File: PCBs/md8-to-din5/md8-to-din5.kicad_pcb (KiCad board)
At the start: 2 copper layers, 32.6 x 28.8 mm, 6 parts, among them J1 DIN-5_180degree_female, J2 Mini-DIN-8_male, J3 RX/TX straight/null, J4 DTR/DSR straight/null

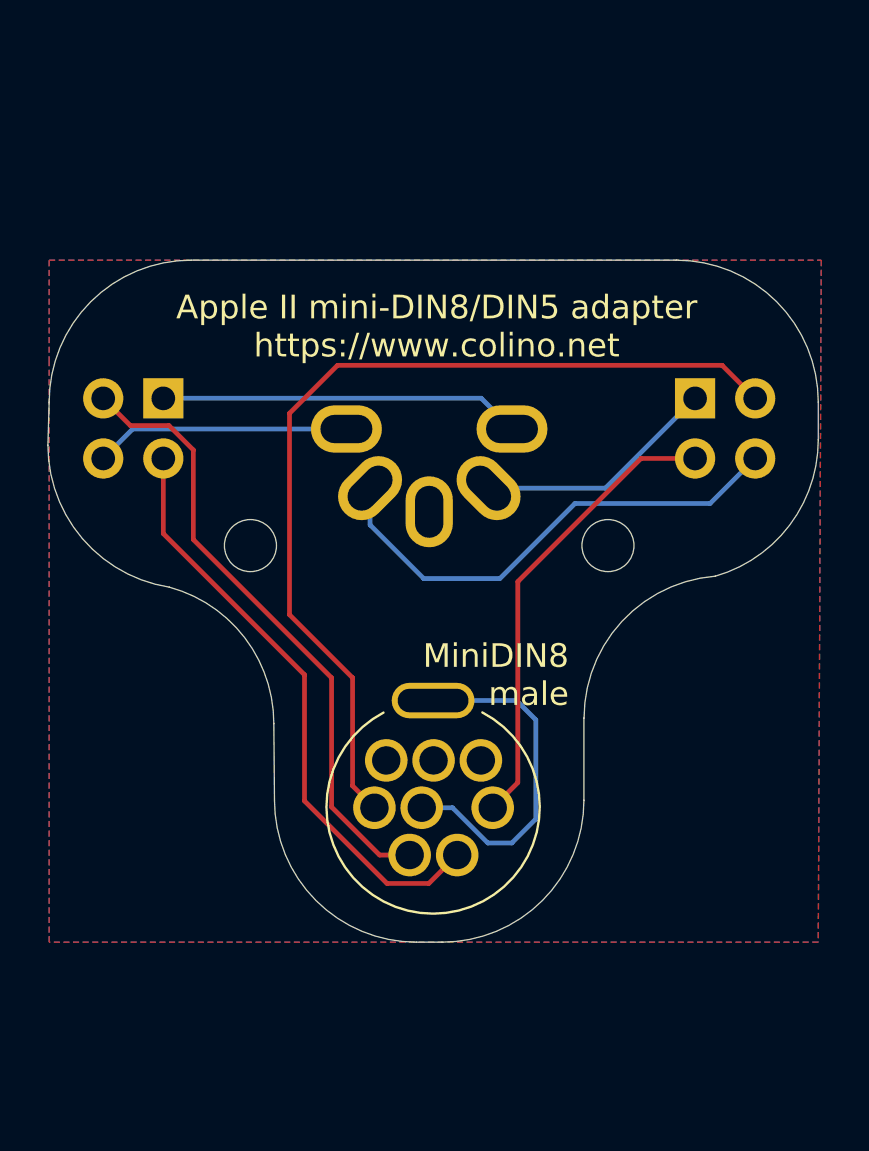
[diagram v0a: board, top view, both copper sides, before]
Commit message: Put traces on the other side of components
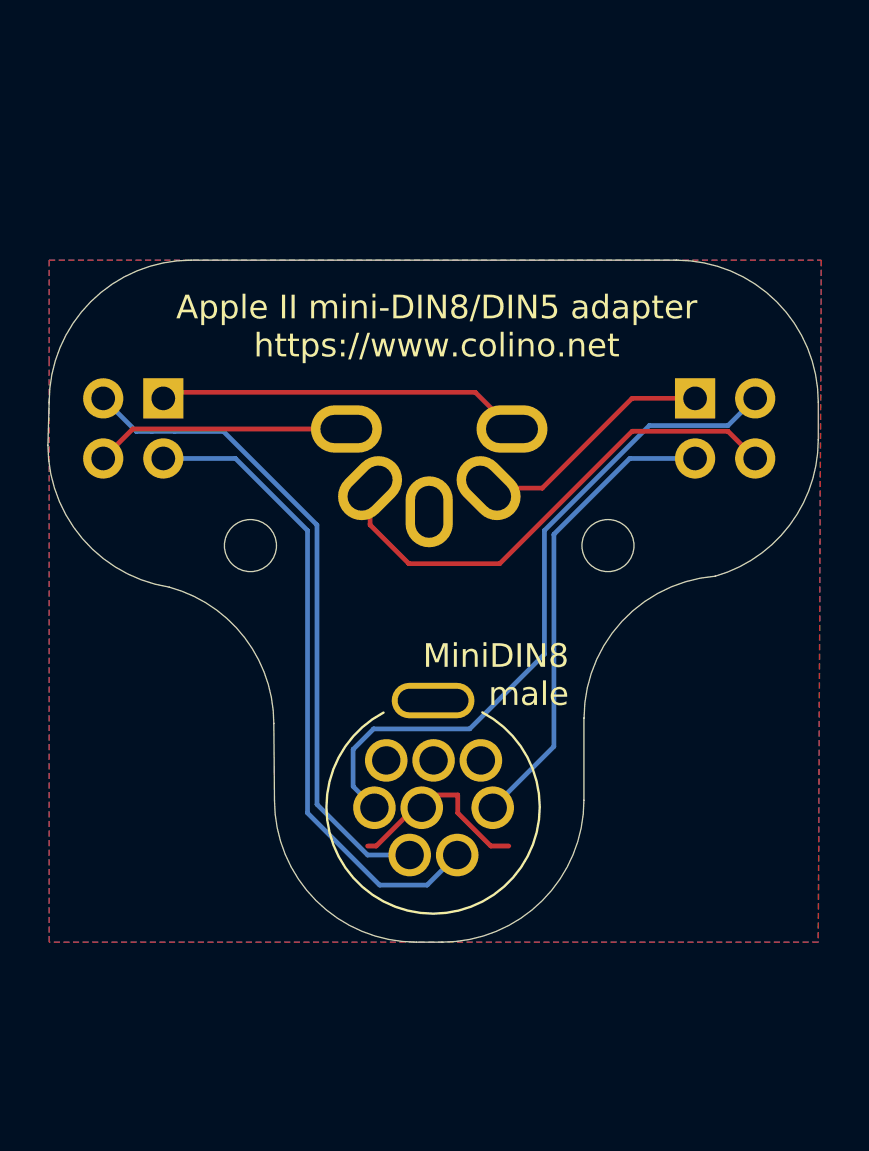
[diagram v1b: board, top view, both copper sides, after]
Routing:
- net Net-(J3-Pin_3): track 39.3 -> 29.0 mm
- net GND: track 14.7 -> 8.20 mm
- net Net-(J4-Pin_3): track 25.3 -> 27.4 mm
- net Net-(J4-Pin_2): track 26.4 -> 27.9 mm

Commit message: Fix silkscreen
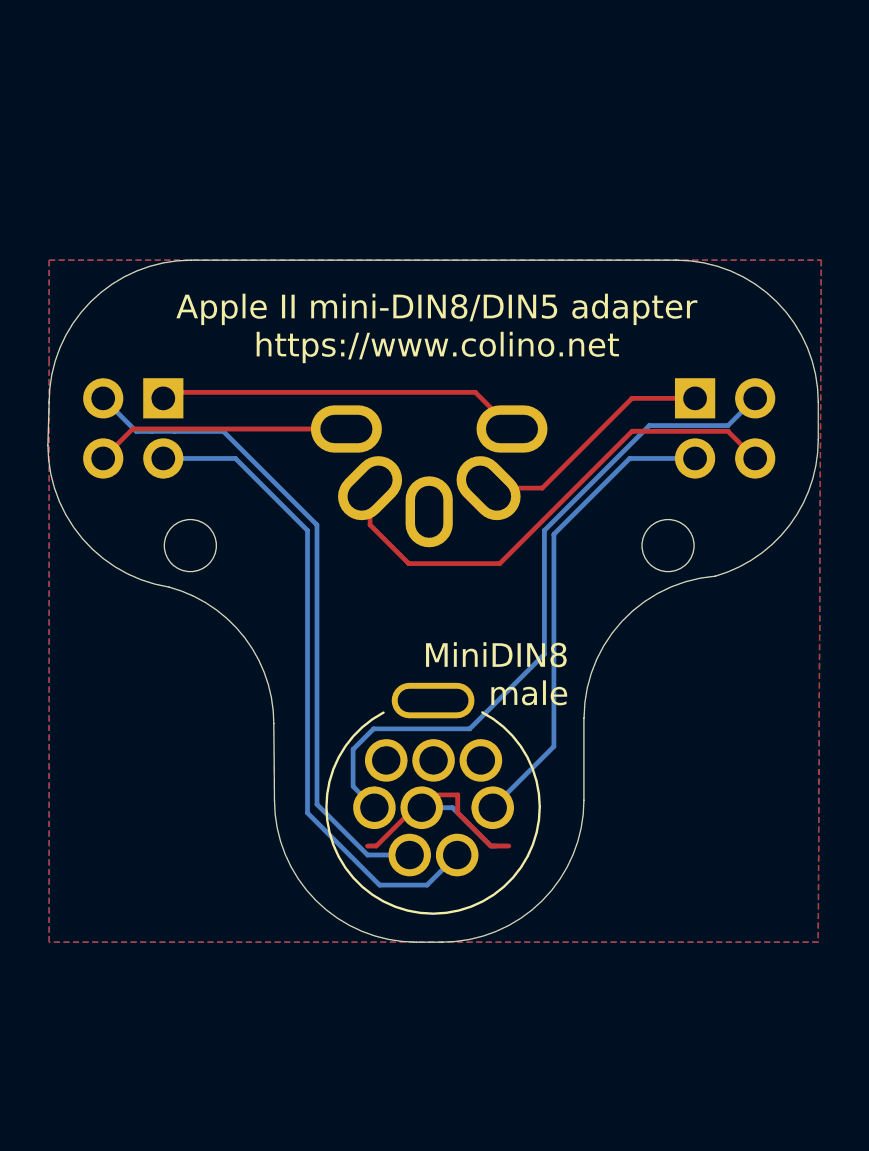
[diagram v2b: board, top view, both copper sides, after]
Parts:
- moved REF** 2.54 mm to (173.7, 97.7)
- moved REF** 2.54 mm to (193.9, 97.7)
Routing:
- net GND: track 8.20 -> 12.0 mm
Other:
- board text added: "↕ straight ↔ cross"
- board text removed: "↔ straight ↕ cross"
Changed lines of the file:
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@@
 	(footprint "MountingHole:MountingHole_2.2mm_M2_ISO7380"
 		(layer "F.Cu")
-		(at 191.389 97.663)
+		(at 193.929 97.663)
 		(descr "Mounting Hole 2.2mm, no annular, M2, ISO7380")
 		(tags "mounting hole 2.2mm no annular m2 iso7380")
@@
 	(footprint "MountingHole:MountingHole_2.2mm_M2_ISO7380"
 		(layer "F.Cu")
-		(at 176.276 97.663)
+		(at 173.736 97.663)
 		(descr "Mounting Hole 2.2mm, no annular, M2, ISO7380")
 		(tags "mounting hole 2.2mm no annular m2 iso7380")
@@
 		)
 	)
-	(gr_text "↔ straight\n↕ cross"
+	(gr_text "↕ straight\n↔ cross"
 		(at 196.342 89.408 0)
 		(layer "B.SilkS")
@@
 		(net 12)
 	)
+	(segment
+		(start 186.438943 110.363)
+		(end 186.69 110.363)
+		(width 0.2)
+		(layer "B.Cu")
+		(net 12)
+	)
+	(segment
+		(start 184.819943 108.744)
+		(end 186.438943 110.363)
+		(width 0.2)
+		(layer "B.Cu")
+		(net 12)
+	)
+	(segment
+		(start 183.517 108.744)
+		(end 184.819943 108.744)
+		(width 0.2)
+		(layer "B.Cu")
+		(net 12)
+	)

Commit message: Rework form factor for IIgs compatibility
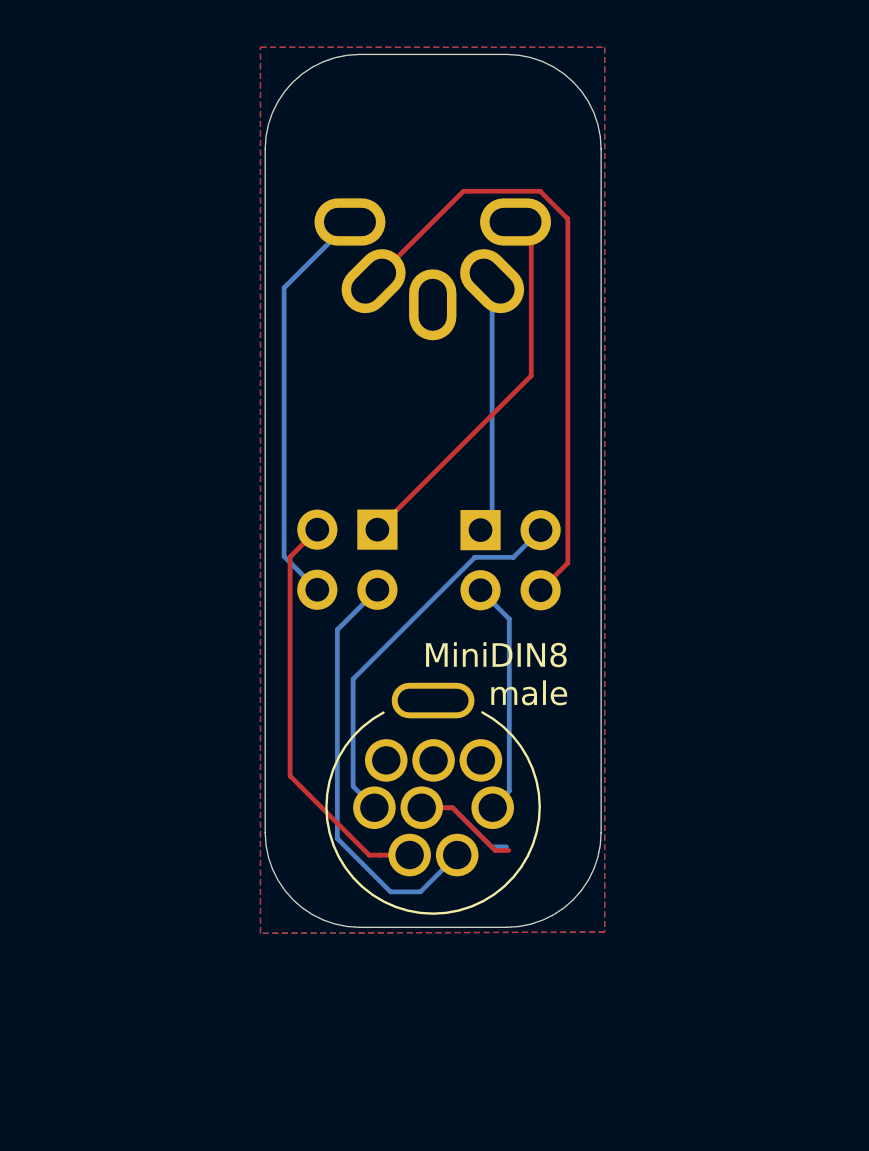
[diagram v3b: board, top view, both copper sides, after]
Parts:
- removed REF** (x2): MountingHole_2.2mm_M2_ISO7380, MountingHole:MountingHole_2.2mm_M2_ISO7380
- moved J3 10.6 mm to (186.0, 97.0)
- moved J4 10.6 mm to (181.6, 97.0)
- moved J1 8.75 mm to (184.0, 87.5)
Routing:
- net Net-(J3-Pin_3): track 29.0 -> 16.3 mm
- net Net-(J4-Pin_2): track 27.9 -> 17.3 mm
- net Net-(J3-Pin_2): track 19.9 -> 9.99 mm
- net Net-(J4-Pin_3): track 27.4 -> 17.9 mm
- net Net-(J4-Pin_4): track 10.8 -> 17.3 mm
- net Net-(J3-Pin_4): track 21.3 -> 26.4 mm
- net GND: track 12.0 -> 8.70 mm
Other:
- board size 32.6 x 28.8 mm -> 14.2 x 36.9 mm
- board text removed: "Apple II mini-DIN8/DIN5 adapter https://www.colino.net"

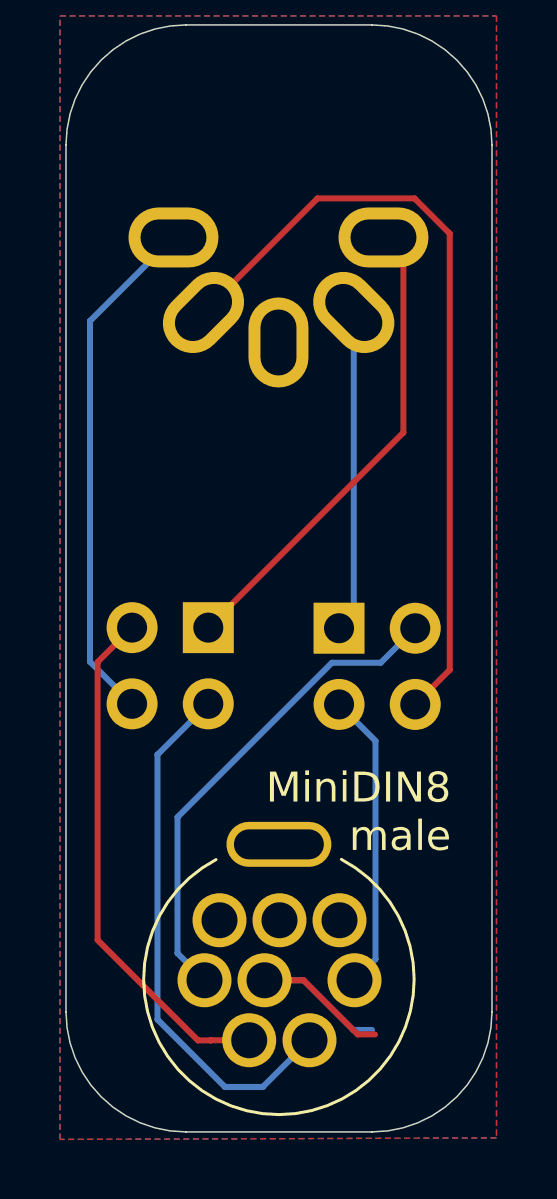
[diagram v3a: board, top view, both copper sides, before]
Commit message: Add switch to CISD
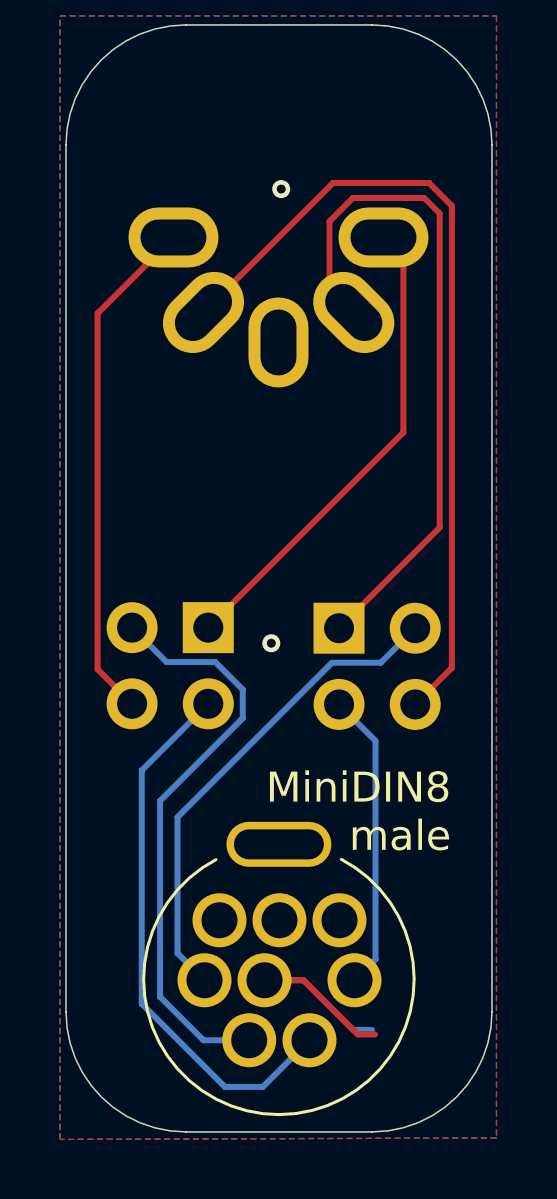
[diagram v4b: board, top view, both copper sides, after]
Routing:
- net Net-(J3-Pin_1): track 10.7 -> 22.8 mm
- net Net-(J4-Pin_2): track 17.3 -> 19.5 mm
- net Net-(J3-Pin_4): track 26.4 -> 27.5 mm
- net GND: vias 0 -> 2
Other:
- board text added: "↔ straight ↕ cross"
- board text removed: "↕ straight ↔ cross"
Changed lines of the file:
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@@
 		)
 	)
-	(gr_text "↕ straight\n↔ cross"
+	(gr_text "↔ straight\n↕ cross"
 		(at 189.7 93.55 0)
 		(layer "B.SilkS")
@@
 	)
 	(segment
-		(start 177.953 98.14)
+		(start 182.793 100.006346)
+		(end 182.793 99.053654)
+		(width 0.2)
+		(layer "B.Cu")
+		(net 3)
+	)
+	(segment
+		(start 181.879346 98.14)
+		(end 180.253 98.14)
+		(width 0.2)
+		(layer "B.Cu")
+		(net 3)
+	)
+	(segment
+		(start 183.007 110.744)
+		(end 181.483 110.744)
+		(width 0.2)
+		(layer "B.Cu")
+		(net 3)
+	)
+	(segment
+		(start 180.0352 109.2962)
+		(end 180.0352 102.764146)
+		(width 0.2)
+		(layer "B.Cu")
+		(net 3)
+	)
+	(segment
+		(start 180.253 98.14)
 		(end 179.103 96.99)
 		(width 0.2)
-		(layer "F.Cu")
-		(net 3)
-	)
-	(segment
-		(start 177.953 107.403)
-		(end 177.953 98.14)
-		(width 0.2)
-		(layer "F.Cu")
-		(net 3)
-	)
-	(segment
-		(start 183.007 110.744)
-		(end 181.734208 110.744)
-		(width 0.2)
-		(layer "F.Cu")
-		(net 3)
-	)
-	(segment
-		(start 181.734208 110.744)
-		(end 181.728208 110.75)
-		(width 0.2)
-		(layer "F.Cu")
-		(net 3)
-	)
-	(segment
-		(start 181.728208 110.75)
-		(end 181.3 110.75)
-		(width 0.2)
-		(layer "F.Cu")
-		(net 3)
-	)
-	(segment
-		(start 181.3 110.75)
-		(end 177.953 107.403)
-		(width 0.2)
-		(layer "F.Cu")
-		(net 3)
-	)
-	(segment
-		(start 181.643 99.53)
-		(end 179.95 101.223)
+		(layer "B.Cu")
+		(net 3)
+	)
+	(segment
+		(start 182.793 99.053654)
+		(end 181.879346 98.14)
+		(width 0.2)
+		(layer "B.Cu")
+		(net 3)
+	)
+	(segment
+		(start 180.0352 102.764146)
+		(end 182.793 100.006346)
+		(width 0.2)
+		(layer "B.Cu")
+		(net 3)
+	)
+	(segment
+		(start 181.483 110.744)
+		(end 180.0352 109.2962)
+		(width 0.2)
+		(layer "B.Cu")
+		(net 3)
+	)
+	(segment
+		(start 179.4256 109.5256)
+		(end 182.2 112.3)
 		(width 0.2)
 		(layer "B.Cu")
@@
 	)
 	(segment
+		(start 179.4256 101.7474)
+		(end 179.4256 109.5256)
+		(width 0.2)
+		(layer "B.Cu")
+		(net 5)
+	)
+	(segment
 		(start 182.2 112.3)
 		(end 183.461 112.3)
@@
 	)
 	(segment
-		(start 179.95 101.223)
-		(end 179.95 110.05)
-		(width 0.2)
-		(layer "B.Cu")
-		(net 5)
-	)
-	(segment
-		(start 179.95 110.05)
-		(end 182.2 112.3)
+		(start 181.643 99.53)
+		(end 179.4256 101.7474)
 		(width 0.2)
 		(layer "B.Cu")
@@
 	(segment
 		(start 180.482457 83.984639)
-		(end 177.7 86.767096)
-		(width 0.2)
-		(layer "B.Cu")
+		(end 177.953 86.514096)
+		(width 0.2)
+		(layer "F.Cu")
 		(net 6)
 	)
 	(segment
-		(start 177.7 86.767096)
-		(end 177.7 98.127)
-		(width 0.2)
-		(layer "B.Cu")
+		(start 177.953 86.514096)
+		(end 177.953 98.38)
+		(width 0.2)
+		(layer "F.Cu")
 		(net 6)
 	)
 	(segment
-		(start 177.7 98.127)
+		(start 177.953 98.38)
 		(end 179.103 99.53)
 		(width 0.2)
-		(layer "B.Cu")
+		(layer "F.Cu")
 		(net 6)
 	)
 	(segment
-		(start 189.691611 98.4)
+		(start 185.798096 82.169)
+		(end 189.0014 82.169)
+		(width 0.2)
+		(layer "F.Cu")
+		(net 7)
+	)
+	(segment
+		(start 189.0014 82.169)
+		(end 189.7634 82.931)
+		(width 0.2)
+		(layer "F.Cu")
+		(net 7)
+	)
+	(segment
+		(start 189.7634 82.931)
+		(end 189.7634 98.328211)
+		(width 0.2)
+		(layer "F.Cu")
+		(net 7)
+	)
+	(segment
+		(start 181.482457 86.484639)
+		(end 185.798096 82.169)
+		(width 0.2)
+		(layer "F.Cu")
+		(net 7)
+	)
+	(segment
+		(start 189.7634 98.328211)
 		(end 188.541611 99.55)
 		(width 0.2)
@@
 	)
 	(segment
-		(start 181.482457 86.484639)
-		(end 185.282457 82.684639)
-		(width 0.2)
-		(layer "F.Cu")
-		(net 7)
-	)
-	(segment
-		(start 185.282457 82.684639)
-		(end 188.520935 82.684639)
-		(width 0.2)
-		(layer "F.Cu")
-		(net 7)
-	)
-	(segment
-		(start 188.520935 82.684639)
-		(end 189.691611 83.855315)
-		(width 0.2)
-		(layer "F.Cu")
-		(net 7)
-	)
-	(segment
-		(start 189.691611 83.855315)
-		(end 189.691611 98.4)
-		(width 0.2)
-		(layer "F.Cu")
-		(net 7)
+		(start 186.460875 82.667743)
+		(end 188.839743 82.667743)
+		(width 0.2)
+		(layer "F.Cu")
+		(net 8)
+	)
+	(segment
+		(start 185.682457 83.446161)
+		(end 186.460875 82.667743)
+		(width 0.2)
+		(layer "F.Cu")
+		(net 8)
+	)
+	(segment
+		(start 188.839743 82.667743)
+		(end 189.357 83.185)
+		(width 0.2)
+		(layer "F.Cu")
+		(net 8)
 	)
 	(segment
 		(start 186.492457 86.484639)
-		(end 186.492457 96.519154)
-		(width 0.2)
-		(layer "B.Cu")
-		(net 8)
-	)
-	(segment
-		(start 186.492457 96.519154)
+		(end 185.682457 85.674639)
+		(width 0.2)
+		(layer "F.Cu")
+		(net 8)
+	)
+	(segment
+		(start 189.357 93.654611)
 		(end 186.001611 97.01)
 		(width 0.2)
-		(layer "B.Cu")
+		(layer "F.Cu")
+		(net 8)
+	)
+	(segment
+		(start 185.682457 85.674639)
+		(end 185.682457 83.446161)
+		(width 0.2)
+		(layer "F.Cu")
+		(net 8)
+	)
+	(segment
+		(start 189.357 83.185)
+		(end 189.357 93.654611)
+		(width 0.2)
+		(layer "F.Cu")
 		(net 8)
 	)
@@
 		(net 12)
 	)
+	(via
+		(at 184.0738 82.3722)
+		(size 0.6)
+		(drill 0.3)
+		(layers "F.Cu" "B.Cu")
+		(free yes)
+		(net 12)
+	)
+	(via
+		(at 183.7436 97.5106)
+		(size 0.6)
+		(drill 0.3)
+		(layers "F.Cu" "B.Cu")
+		(free yes)
+		(net 12)
+	)
